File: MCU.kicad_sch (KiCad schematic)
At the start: 2 parts, among them U3 nRF7002-QFXX, U4 ISP2053-AX

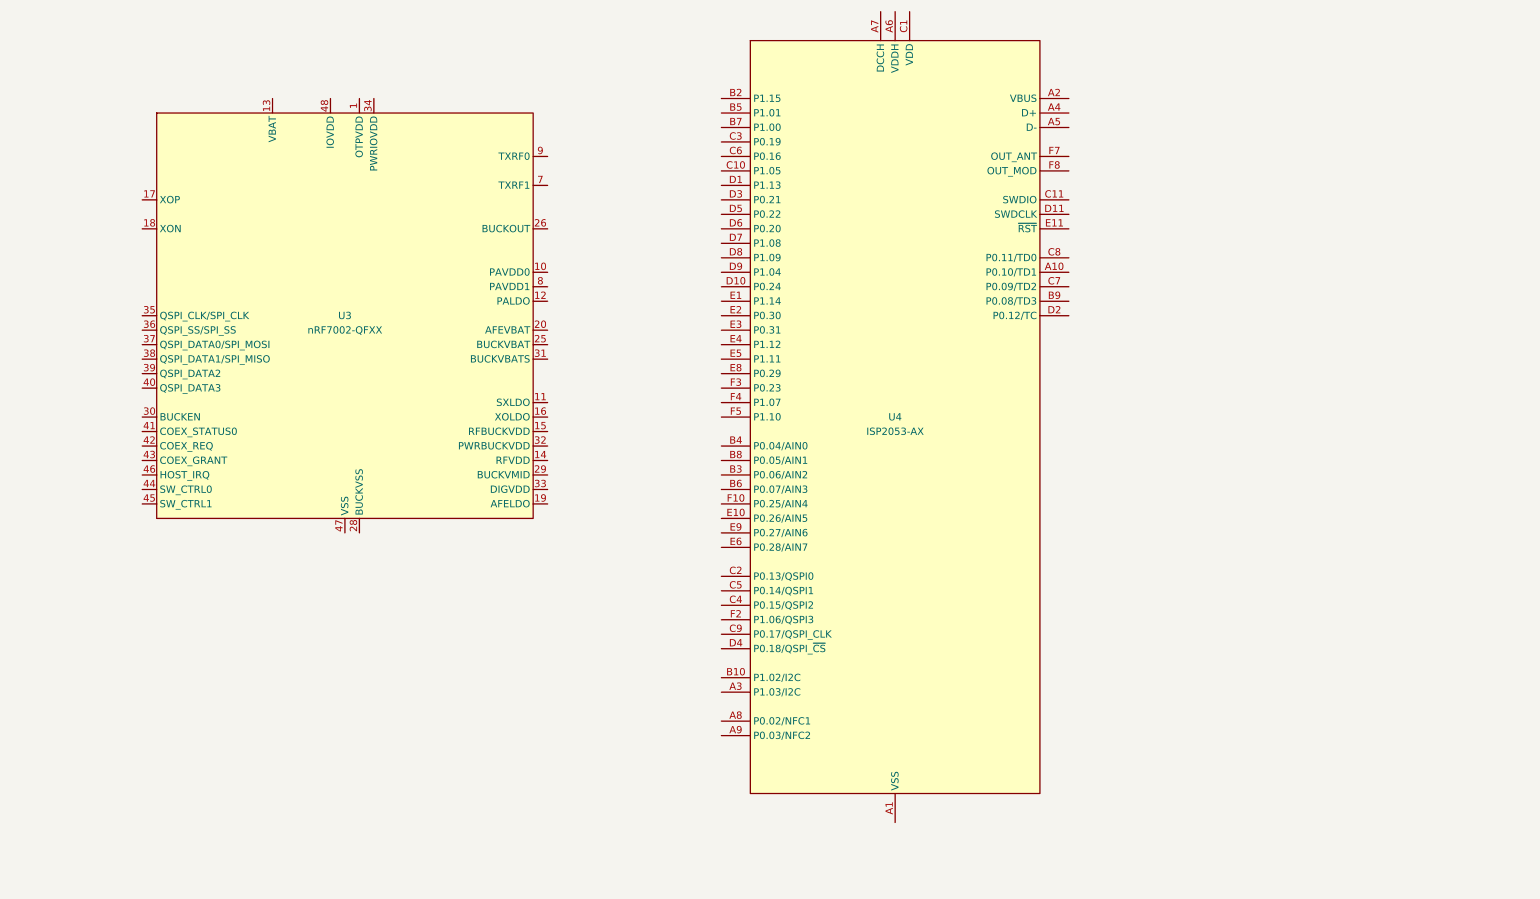
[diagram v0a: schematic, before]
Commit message: Added nrf5340 and pi filters on output of switching supplies
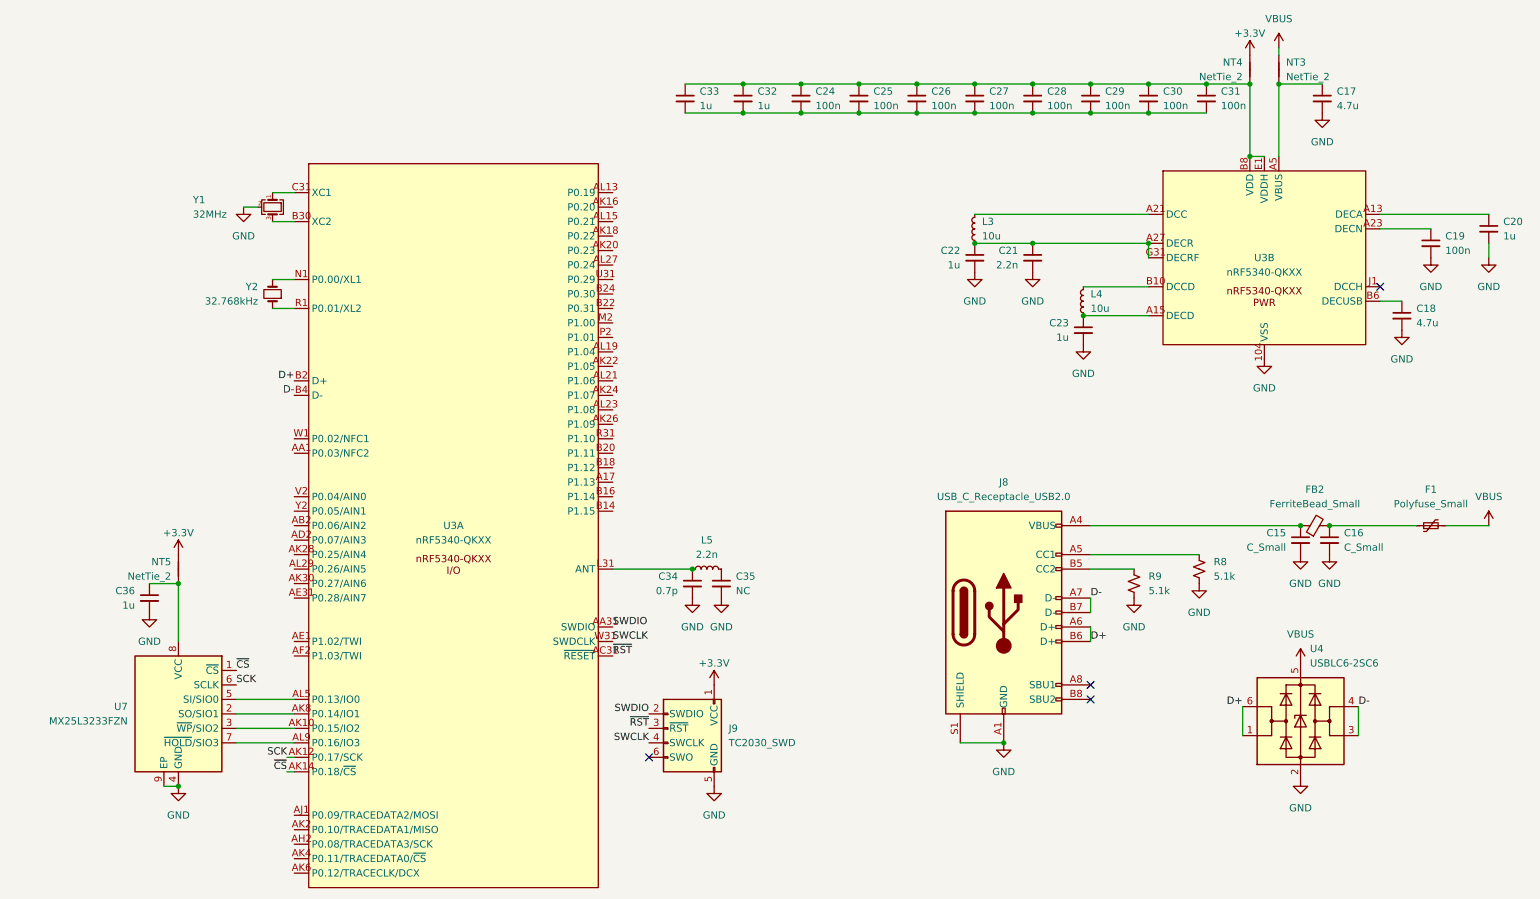
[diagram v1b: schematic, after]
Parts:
- removed U3: nRF7002-QFXX, Package_DFN_QFN:QFN-48-1EP_6x6mm_P0.4mm_EP4.6x4.6mm_ThermalVias, symbol PCM_nordic-lib-kicad-nrf7:nRF7002-QFXX
- removed U4: ISP2053-AX, nordic-lib-kicad-nrf53-modules:ISP2053_8x8mm_LGA, symbol nordic-lib-kicad-nrf53-modules:ISP2053-AX
- added C15, C16: C_Small, symbol Device:C_Small
- added C17, C18: 4.7u, symbol Device:C_Small
- added C19, C24, C25, C26, C27, C28, C29, C30, C31: 100n, symbol Device:C_Small
- added C20, C22, C23, C32, C33, C36: 1u, symbol Device:C_Small
- added C21: 2.2n, symbol Device:C_Small
- added C34: 0.7p, symbol Device:C_Small
- added C35: NC, symbol Device:C_Small
- added F1: Polyfuse_Small, symbol Device:Polyfuse_Small
- added FB2: FerriteBead_Small, symbol Device:FerriteBead_Small
- added J8: USB_C_Receptacle_USB2.0, symbol Connector:USB_C_Receptacle_USB2.0
- added J9: TC2030_SWD, PCM_marbastlib-various:CON_TC2030_outlined, symbol PCM_marbastlib-various:TC2030_SWD
- added L3, L4: 10u, symbol Device:L_Small
- added L5: 2.2n, symbol Device:L_Small
- added NT3, NT4, NT5: NetTie_2, symbol Device:NetTie_2
- added R8, R9: 5.1k, symbol Device:R_Small_US
- added U3: nRF5340-QKXX, PCM_nordic-lib-kicad-nrf53:aQFN-94_7x7mm, symbol PCM_nordic-lib-kicad-nrf53:nRF5340-QKXX
- added U4: USBLC6-2SC6, Package_TO_SOT_SMD:SOT-23-6, symbol Power_Protection:USBLC6-2SC6
- added U7: MX25L3233FZN, Package_SON:WSON-8-1EP_6x5mm_P1.27mm_EP3.4x4mm, symbol Memory_Flash:MX25L3233FZN
- added Y1: 32MHz, symbol EasyCrystal:Crystal_GND24_Small_EZ
- added Y2: 32.768kHz, symbol Device:Crystal_Small
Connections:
- new net: C20.1, U3.A13 (DECA)
- new net: L4.1, U3.B10 (DCCD)
- new net: C23.1, L4.2, U3.A15 (DECD)
- new net: C24.1, C25.1, C26.1, C27.1, C28.1, C29.1, C30.1, C31.1, C32.1, C33.1, NT4.1, U3.A19 (VDD), U3.AC1 (VDD), U3.AG1 (VDD), U3.AJ31 (VDD), U3.AL11 (VDD), U3.AL17 (VDD), U3.AL25 (VDD), U3.AL3 (VDD), U3.AL7 (VDD), U3.B28 (VDD), U3.B8 (VDD), U3.C1 (VDD), U3.E1 (VDDH), U3.E31 (VDD), U3.L1 (VDD), U3.N31 (VDD), U3.U1 (VDD)
- new net: C24.2, C25.2, C26.2, C27.2, C28.2, C29.2, C30.2, C31.2, C32.2, C33.2
- new net: C21.1, C22.1, L3.2, U3.A27 (DECR), U3.G31 (DECRF)
- new net: C16.1, F1.1, FB2.2
- new net: C35.1, L5.1
- new net: C36.1, NT5.1, U7.8 (VCC)
- new net: C15.1, FB2.1, J8.A4 (VBUS), J8.A9 (VBUS), J8.B4 (VBUS), J8.B9 (VBUS)
- new net: J8.A5 (CC1), R8.1
- new net: J8.B5 (CC2), R9.1
- new net: C34.1, L5.2, U3.L31 (ANT)
- new net: L3.1, U3.A21 (DCC)
- new net: C19.1, U3.A23 (DECN)
- new net: C17.1, NT3.1, U3.A5 (VBUS)
- new net: C18.1, U3.B6 (DECUSB)
- new net: U3.C31 (XC1), Y1.1
- new net: U3.B30 (XC2), Y1.3
- new net: U3.R1 (P0.01/XL2), Y2.1
- new net: U3.N1 (P0.00/XL1), Y2.2
- new net: U3.AK8 (P0.14/IO1), U7.2 (SO/SIO1)
- new net: U3.AK10 (P0.15/IO2), U7.3 (~{WP}/SIO2)
- new net: U3.AL5 (P0.13/IO0), U7.5 (SI/SIO0)
- new net: U3.AL9 (P0.16/IO3), U7.7 (~{HOLD}/SIO3)
- new net +3.3V: J9.1 (VCC), NT4.2, NT5.2
- new net D+: J8.A6 (D+), J8.B6 (D+), U3.B2 (D+), U4.1 (I/O1), U4.6 (I/O1)
- new net D-: J8.A7 (D-), J8.B7 (D-), U3.B4 (D-), U4.3 (I/O2), U4.4 (I/O2)
- new net GND: C15.2, C16.2, C17.2, C18.2, C19.2, C20.2, C21.2, C22.2, C23.2, C34.2, C35.2, C36.2, J8.A1 (GND), J8.A12 (GND), J8.B1 (GND), J8.B12 (GND), J8.S1 (SHIELD), J9.5 (GND), R8.2, R9.2, U3.104 (VSS), U4.2 (GND), U7.4 (GND), U7.9 (EP), Y1.2, Y1.4
- new net SCK: U3.AK12 (P0.17/SCK), U7.6 (SCLK)
- new net SWCLK: J9.4 (SWCLK), U3.W31 (SWDCLK)
- new net SWDIO: J9.2 (SWDIO), U3.AA31 (SWDIO)
- new net VBUS: F1.2, NT3.2, U4.5 (VBUS)
- new net ~{CS}: U3.AK14 (P0.18/~{CS}), U7.1 (~{CS})
- new net ~{RST}: J9.3 (~{RST}), U3.AC31 (~{RESET})
- no-connect marks 0 -> 4

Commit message: 10/09/23 - Schematic v0.1
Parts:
- added J10: Conn_01x02, RF_Antenna:Texas_SWRA117D_2.4GHz_Left, symbol Connector_Generic:Conn_01x02
- added TP1: UART_TX, TestPoint:TestPoint_Keystone_5015_Micro-Minature, symbol Connector:TestPoint_Small
- added TP2: UART_RX, TestPoint:TestPoint_Keystone_5015_Micro-Minature, symbol Connector:TestPoint_Small
- C15, C16: value C_Small -> 100n
- C34, C35: footprint (none) -> Capacitor_SMD:C_0201_0603Metric
- C36, L5: footprint (none) -> Inductor_SMD:L_0201_0603Metric
- F1: value Polyfuse_Small -> 500mA
- FB2: value FerriteBead_Small -> 100R @ 100 MHz
- J8: footprint (none) -> Connector_USB:USB_C_Receptacle_HRO_TYPE-C-31-M-12
- NT3, NT4, NT5: footprint (none) -> NetTie:NetTie-2_SMD_Pad0.5mm
- R8, R9: footprint (none) -> Resistor_SMD:R_0402_1005Metric
- Y1: footprint (none) -> Crystal:Crystal_SMD_2016-4Pin_2.0x1.6mm; MPN (none) -> ECS-320-8-37B2-7KM-TR
- Y2: footprint (none) -> Crystal:Crystal_SMD_2012-2Pin_2.0x1.2mm; MMPN (none) -> ECS-.327-9-12R-TR
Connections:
- net GND: now also J10.1 (Pin_1)
- net VBUS: no longer U4.5 (VBUS)
- net at C35.1, L5.1: now also J10.2 (Pin_2)
- net VBUS_ESD: now reaches C15.1, FB2.1, J8.A4 (VBUS), J8.A9 (VBUS), J8.B4 (VBUS), J8.B9 (VBUS)
- net VBUS_ESD: now also U4.5 (VBUS)
- net at U3.AK16 (P0.20): now also TP2.1
- net at U3.AL13 (P0.19): now also TP1.1

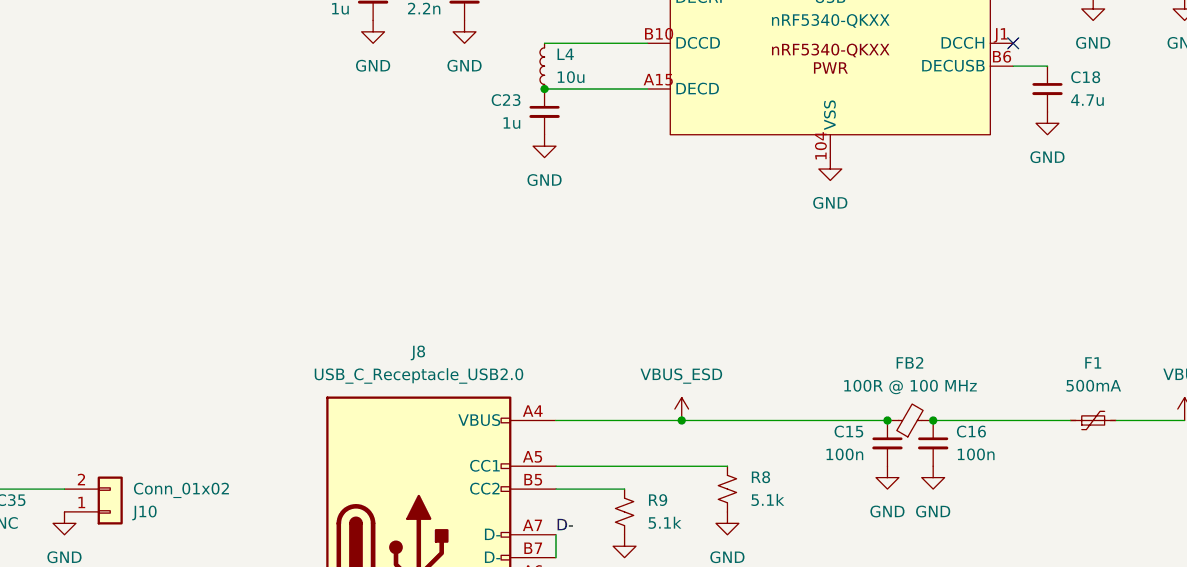
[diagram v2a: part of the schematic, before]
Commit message: Modified README, added image, fixed schematic
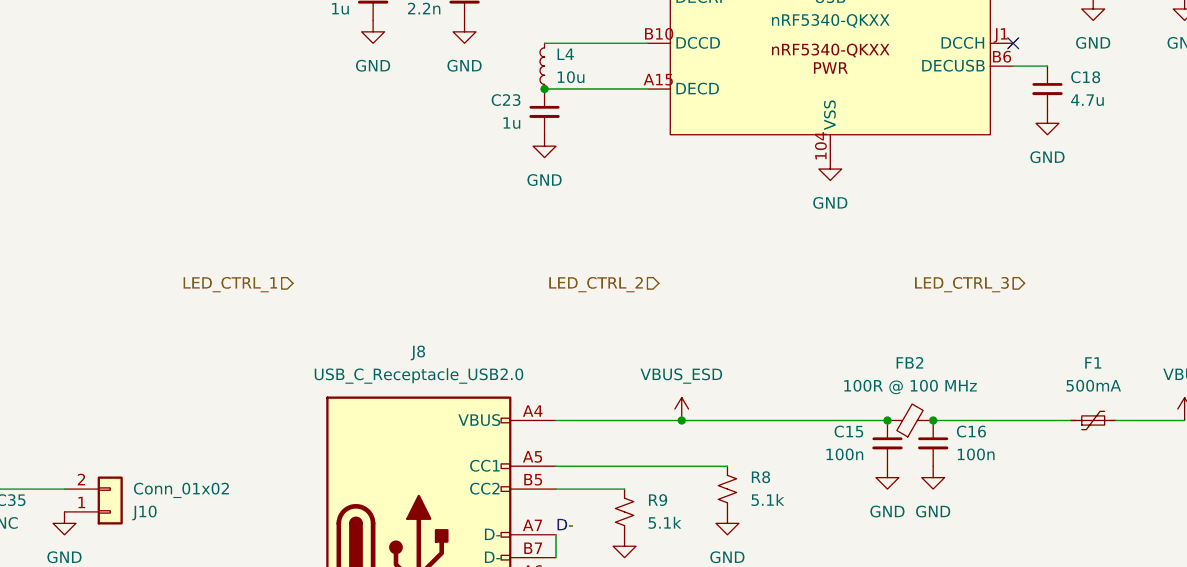
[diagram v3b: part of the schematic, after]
